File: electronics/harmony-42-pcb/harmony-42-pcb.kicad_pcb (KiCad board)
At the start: 2 copper layers, 285.8 x 133.3 mm, 84 parts

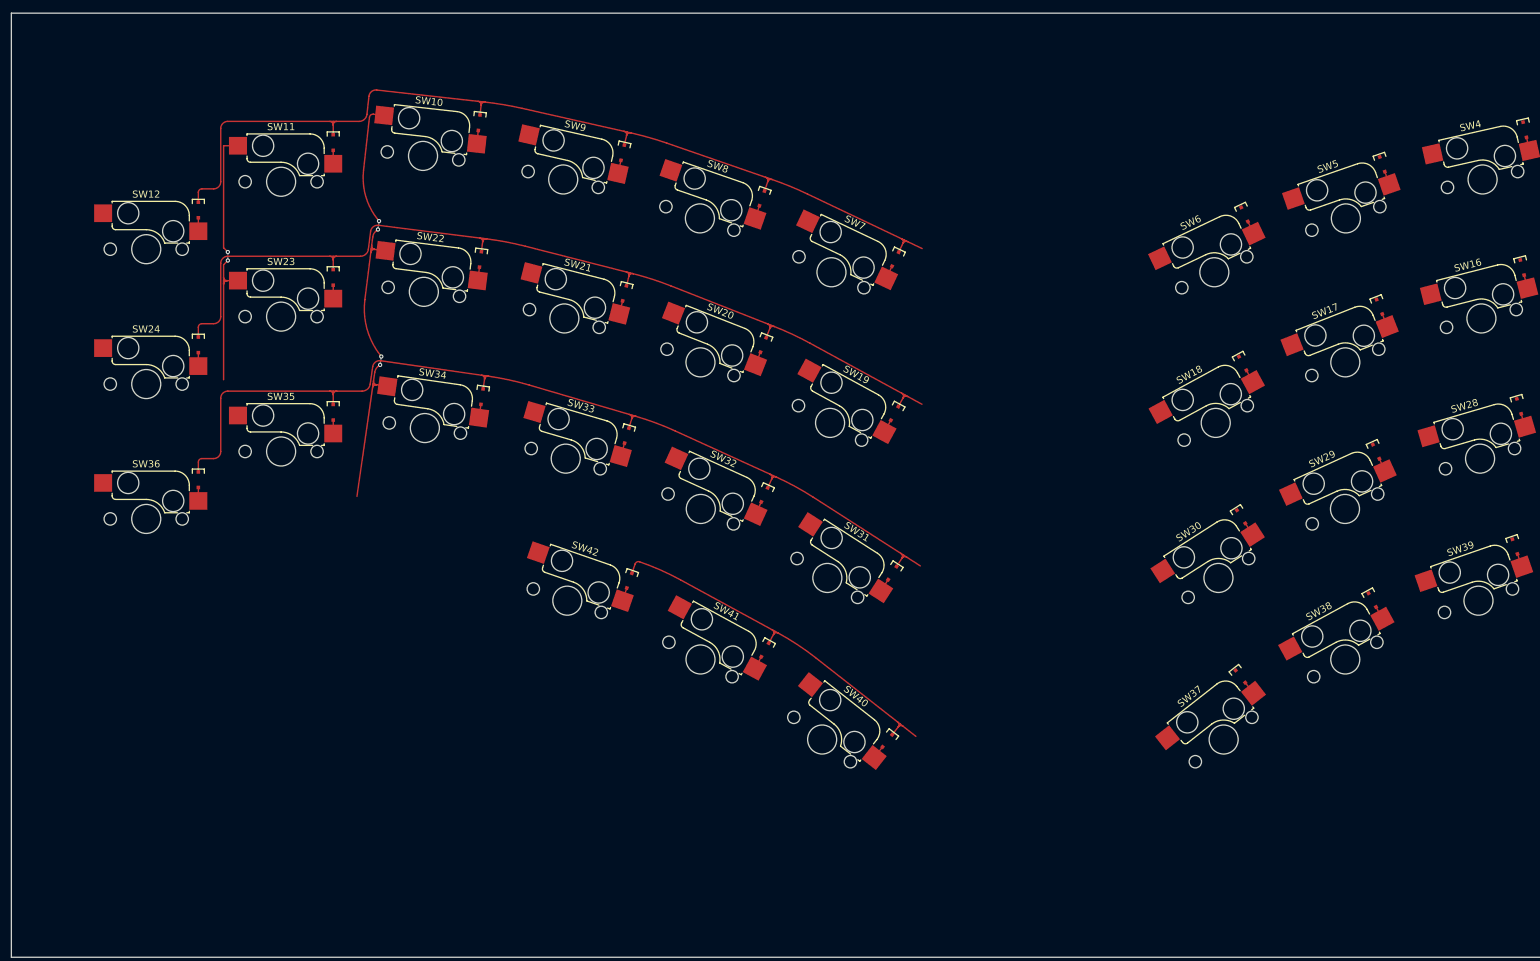
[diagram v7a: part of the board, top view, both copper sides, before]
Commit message: Add routes
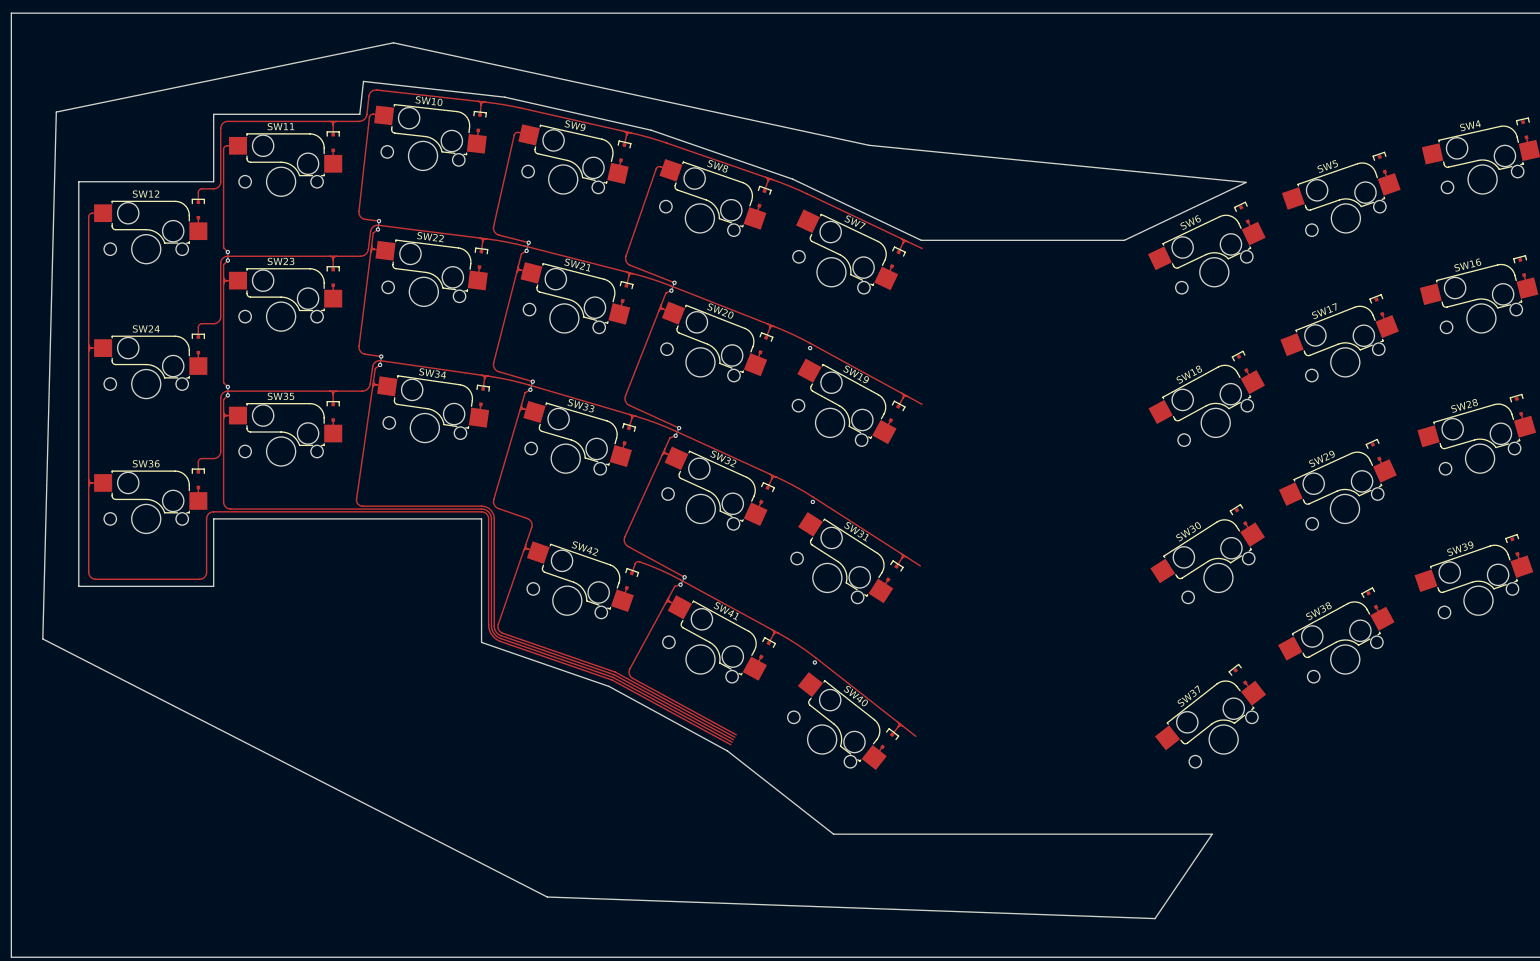
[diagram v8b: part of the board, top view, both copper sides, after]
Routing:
- net Net-(SW20-Pad1): track 0.00 -> 3.60 mm, vias 0 -> 6
- net Net-(SW21-Pad1): track 0.00 -> 2.40 mm, vias 0 -> 4
- net Net-(SW11-Pad1): track 1.20 -> 2.40 mm, vias 2 -> 5
- net Net-(D37-K): vias 0 -> 1
- net Net-(D25-K): vias 0 -> 1
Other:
- outline, holes or cut-outs redrawn
